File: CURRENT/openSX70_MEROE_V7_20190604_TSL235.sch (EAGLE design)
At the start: 43 parts, among them J1 687106183722, Q1 5.8A/30V/35mΩ, Q2 5.8A/30V/35mΩ, U1 ATMEGA328P_TQFP, U2 TPS79501DCQ, Y1 CSTCE8M00G52Z-R0

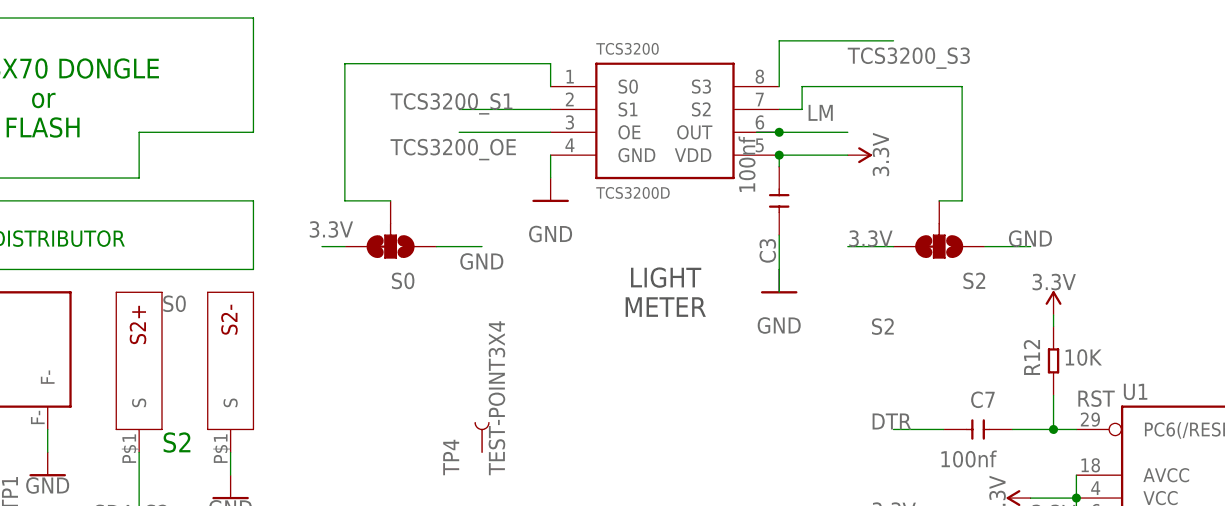
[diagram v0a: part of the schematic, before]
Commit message: TSL235 test
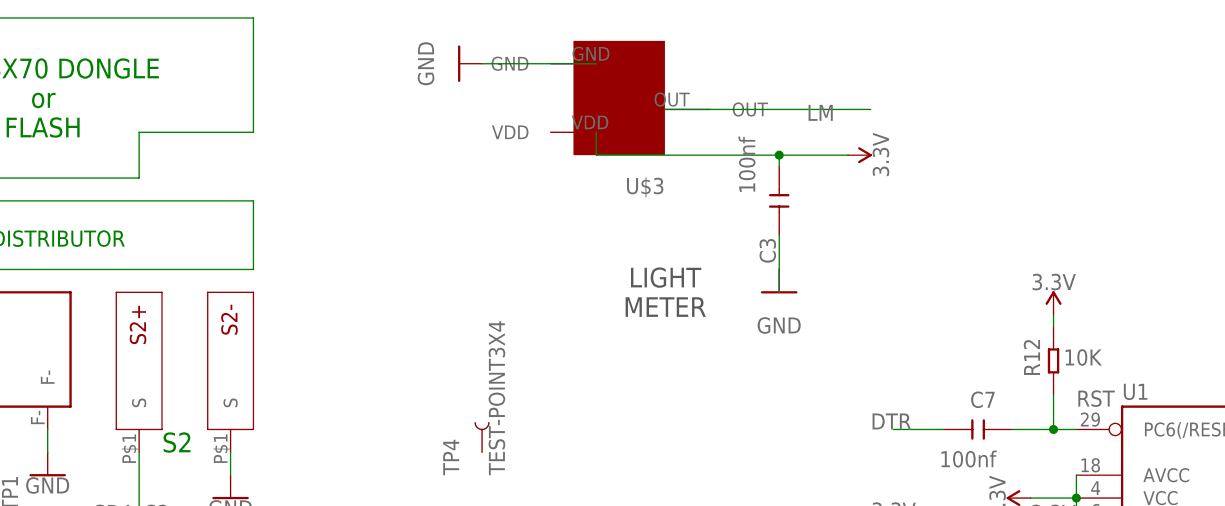
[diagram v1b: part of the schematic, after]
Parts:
- removed S0: S0, SparkFun-Jumpers:JUMPER-SMT_3_1-NC_TRACE_SILK
- removed S2: S2, SparkFun-Jumpers:JUMPER-SMT_3_1-NC_TRACE_SILK
- removed TCS3200: TCS3200D, TCS3200D:TCS3200D
- added U$3: TSL235R, _openSX70:TSL235R
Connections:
- removed net N$7: S0.2, TCS3200.S0
- removed net N$8: S2.2, TCS3200.S2
- net 3.3V: now also U$3.VDD; no longer S0.3, S2.3, TCS3200.VDD
- net GND: now also U$3.GND; no longer S0.1, S2.1, TCS3200.GND
- net LM: now also U$3.OUT; no longer TCS3200.OUT
- net TCS3200_OE: no longer TCS3200.OE
- net TCS3200_S1: no longer TCS3200.S1
- net TCS3200_S3: no longer TCS3200.S3
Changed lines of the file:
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@@
 <part name="TP3" library="SparkFun-Connectors" deviceset="TEST-POINT" device="3X4" value="TEST-POINT3X4"/>
 <part name="TP4" library="SparkFun-Connectors" deviceset="TEST-POINT" device="3X4" value="TEST-POINT3X4"/>
-<part name="TCS3200" library="TCS3200D" deviceset="TCS3200D" device=""/>
 <part name="SUPPLY1" library="SparkFun-PowerSymbols" deviceset="3.3V" device=""/>
-<part name="S2" library="SparkFun-Jumpers" deviceset="JUMPER-SMT_3_1-NC_TRACE" device="_SILK" value="S2"/>
-<part name="S0" library="SparkFun-Jumpers" deviceset="JUMPER-SMT_3_1-NC_TRACE" device="_SILK" value="S0"/>
 <part name="C3" library="Seeed-Capacitor" deviceset="CERAMIC-100NF-50V-10%-X7R(0603)" device="" value="100nf"/>
 <part name="GND19" library="SparkFun-PowerSymbols" deviceset="GND" device=""/>
+<part name="U$3" library="_openSX70" library_urn="urn:adsk.eagle:library:7902803" deviceset="TSL235R" device=""/>
 </parts>
 <sheets>
@@
 <attribute name="VALUE" x="122.174" y="157.48" size="1.778" layer="96" rot="R270" align="bottom-center"/>
 </instance>
-<instance part="GND15" gate="1" x="86.36" y="152.4" smashed="yes">
-<attribute name="VALUE" x="86.36" y="149.606" size="1.778" layer="96" align="top-center"/>
+<instance part="GND15" gate="1" x="76.2" y="167.64" smashed="yes" rot="R270">
+<attribute name="VALUE" x="73.406" y="167.64" size="1.778" layer="96" rot="R270" align="top-center"/>
 </instance>
 <instance part="R11" gate="G$1" x="15.24" y="10.16" smashed="yes" rot="R180">
@@
 <attribute name="VALUE" x="81.28" y="121.92" size="1.778" layer="96" font="vector" rot="R90"/>
 </instance>
-<instance part="TCS3200" gate="G$1" x="96.52" y="160.02" smashed="yes">
-<attribute name="NAME" x="91.43891875" y="168.657840625" size="1.27026875" layer="95"/>
-<attribute name="VALUE" x="91.435940625" y="152.648109375" size="1.27101875" layer="96"/>
-</instance>
 <instance part="SUPPLY1" gate="G$1" x="7.62" y="124.46" smashed="yes" rot="R180">
 <attribute name="VALUE" x="7.62" y="121.666" size="1.778" layer="96" rot="R180" align="bottom-center"/>
-</instance>
-<instance part="S2" gate="G$1" x="129.54" y="147.32" smashed="yes" rot="R270">
-<attribute name="NAME" x="132.08" y="142.621" size="1.778" layer="95" font="vector"/>
-<attribute name="VALUE" x="121.92" y="139.319" size="1.778" layer="96" font="vector" align="top-left"/>
-</instance>
-<instance part="S0" gate="G$1" x="68.58" y="147.32" smashed="yes" rot="R270">
-<attribute name="NAME" x="68.58" y="142.621" size="1.778" layer="95" font="vector"/>
-<attribute name="VALUE" x="43.18" y="141.859" size="1.778" layer="96" font="vector" align="top-left"/>
 </instance>
 <instance part="C3" gate="G$1" x="111.76" y="152.4" smashed="yes" rot="R270">
@@
 <instance part="GND19" gate="1" x="111.76" y="142.24" smashed="yes">
 <attribute name="VALUE" x="111.76" y="139.446" size="1.778" layer="96" align="top-center"/>
+</instance>
+<instance part="U$3" gate="G$1" x="93.98" y="162.56" smashed="yes" rot="R180">
+<attribute name="NAME" x="99.06" y="154.94" size="1.778" layer="95" font="vector" rot="R180"/>
 </instance>
 </instances>
@@
 </segment>
 <segment>
-<pinref part="TCS3200" gate="G$1" pin="VDD"/>
 <pinref part="SUPPLY2" gate="G$1" pin="3.3V"/>
 <wire x1="111.76" y1="157.48" x2="119.38" y2="157.48" width="0.1524" layer="91"/>
 <pinref part="C3" gate="G$1" pin="1"/>
 <wire x1="111.76" y1="157.48" x2="111.76" y2="156.21" width="0.1524" layer="91"/>
+<pinref part="U$3" gate="G$1" pin="VDD"/>
+<wire x1="91.44" y1="160.02" x2="91.44" y2="157.48" width="0.1524" layer="91"/>
+<wire x1="91.44" y1="157.48" x2="111.76" y2="157.48" width="0.1524" layer="91"/>
 <junction x="111.76" y="157.48"/>
 </segment>
@@
 <pinref part="SUPPLY1" gate="G$1" pin="3.3V"/>
 <wire x1="7.62" y1="127" x2="7.62" y2="124.46" width="0.1524" layer="91"/>
-</segment>
-<segment>
-<pinref part="S0" gate="G$1" pin="3"/>
-<wire x1="63.5" y1="147.32" x2="60.96" y2="147.32" width="0.1524" layer="91"/>
-<label x="59.436" y="148.336" size="1.778" layer="95"/>
-</segment>
-<segment>
-<pinref part="S2" gate="G$1" pin="3"/>
-<wire x1="124.46" y1="147.32" x2="119.38" y2="147.32" width="0.1524" layer="91"/>
-<label x="119.38" y="147.32" size="1.778" layer="95"/>
 </segment>
 </net>
@@
 </segment>
 <segment>
-<pinref part="GND15" gate="1" pin="GND"/>
-<pinref part="TCS3200" gate="G$1" pin="GND"/>
-<wire x1="86.36" y1="154.94" x2="86.36" y2="157.48" width="0.1524" layer="91"/>
-</segment>
-<segment>
-<pinref part="S0" gate="G$1" pin="1"/>
-<wire x1="73.66" y1="147.32" x2="78.74" y2="147.32" width="0.1524" layer="91"/>
-<label x="76.2" y="144.78" size="1.778" layer="95"/>
-</segment>
-<segment>
-<pinref part="S2" gate="G$1" pin="1"/>
-<wire x1="134.62" y1="147.32" x2="139.7" y2="147.32" width="0.1524" layer="91"/>
-<label x="137.16" y="147.32" size="1.778" layer="95"/>
-</segment>
-<segment>
 <pinref part="U$1" gate="G$1" pin="GND"/>
 <wire x1="232.664" y1="88.9" x2="232.918" y2="88.9" width="0.1524" layer="91"/>
@@
 <pinref part="GND19" gate="1" pin="GND"/>
 <wire x1="111.76" y1="144.78" x2="111.76" y2="142.24" width="0.1524" layer="91"/>
+</segment>
+<segment>
+<pinref part="GND15" gate="1" pin="GND"/>
+<pinref part="U$3" gate="G$1" pin="GND"/>
+<wire x1="78.74" y1="167.64" x2="91.44" y2="167.64" width="0.1524" layer="91"/>
 </segment>
 </net>
@@
 <segment>
 <label x="114.808" y="161.29" size="1.778" layer="95"/>
-<wire x1="109.22" y1="160.02" x2="111.76" y2="160.02" width="0.1524" layer="91"/>
-<pinref part="TCS3200" gate="G$1" pin="OUT"/>
-<wire x1="111.76" y1="160.02" x2="119.38" y2="160.02" width="0.1524" layer="91"/>
-<junction x="111.76" y="160.02"/>
+<pinref part="U$3" gate="G$1" pin="OUT"/>
+<wire x1="99.06" y1="162.56" x2="121.92" y2="162.56" width="0.1524" layer="91"/>
 </segment>
 </net>
@@
 <label x="215.9" y="68.58" size="1.778" layer="95"/>
 </segment>
-<segment>
-<pinref part="TCS3200" gate="G$1" pin="S1"/>
-<wire x1="86.36" y1="162.56" x2="76.2" y2="162.56" width="0.1524" layer="91"/>
-<label x="68.58" y="162.56" size="1.778" layer="95"/>
-</segment>
 </net>
 <net name="TCS3200_S3" class="0">
@@
 <label x="215.9" y="63.5" size="1.778" layer="95"/>
 </segment>
-<segment>
-<pinref part="TCS3200" gate="G$1" pin="S3"/>
-<wire x1="111.76" y1="165.1" x2="111.76" y2="170.18" width="0.1524" layer="91"/>
-<wire x1="111.76" y1="170.18" x2="124.46" y2="170.18" width="0.1524" layer="91"/>
-<label x="119.38" y="167.64" size="1.778" layer="95"/>
-</segment>
 </net>
 <net name="TCS3200_OE" class="0">
@@
 <label x="215.9" y="58.42" size="1.778" layer="95"/>
 </segment>
-<segment>
-<pinref part="TCS3200" gate="G$1" pin="OE"/>
-<wire x1="86.36" y1="160.02" x2="76.2" y2="160.02" width="0.1524" layer="91"/>
-<label x="68.58" y="157.48" size="1.778" layer="95"/>
-</segment>
-</net>
-<net name="N$7" class="0">
-<segment>
-<pinref part="TCS3200" gate="G$1" pin="S0"/>
-<wire x1="86.36" y1="165.1" x2="86.36" y2="167.64" width="0.1524" layer="91"/>
-<wire x1="86.36" y1="167.64" x2="63.5" y2="167.64" width="0.1524" layer="91"/>
-<wire x1="63.5" y1="167.64" x2="63.5" y2="152.4" width="0.1524" layer="91"/>
-<pinref part="S0" gate="G$1" pin="2"/>
-<wire x1="63.5" y1="152.4" x2="68.58" y2="152.4" width="0.1524" layer="91"/>
-</segment>
-</net>
-<net name="N$8" class="0">
-<segment>
-<pinref part="TCS3200" gate="G$1" pin="S2"/>
-<wire x1="111.76" y1="162.56" x2="114.3" y2="162.56" width="0.1524" layer="91"/>
-<wire x1="114.3" y1="162.56" x2="114.3" y2="165.1" width="0.1524" layer="91"/>
-<wire x1="114.3" y1="165.1" x2="132.08" y2="165.1" width="0.1524" layer="91"/>
-<wire x1="132.08" y1="165.1" x2="132.08" y2="152.4" width="0.1524" layer="91"/>
-<pinref part="S2" gate="G$1" pin="2"/>
-<wire x1="132.08" y1="152.4" x2="129.54" y2="152.4" width="0.1524" layer="91"/>
-</segment>
-</net>
+</net>
